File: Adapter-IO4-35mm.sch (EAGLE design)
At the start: 3 parts

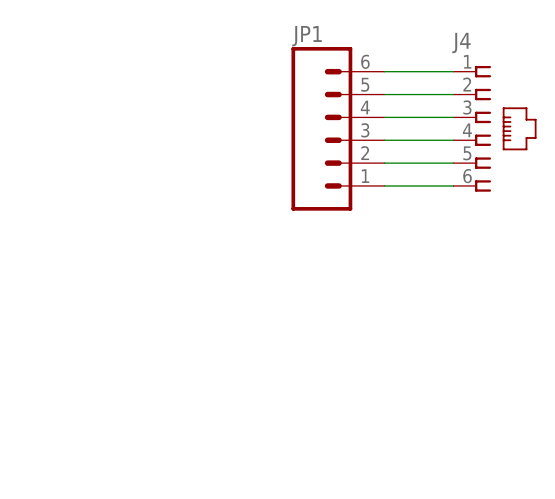
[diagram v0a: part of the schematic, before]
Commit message: added values for connectors
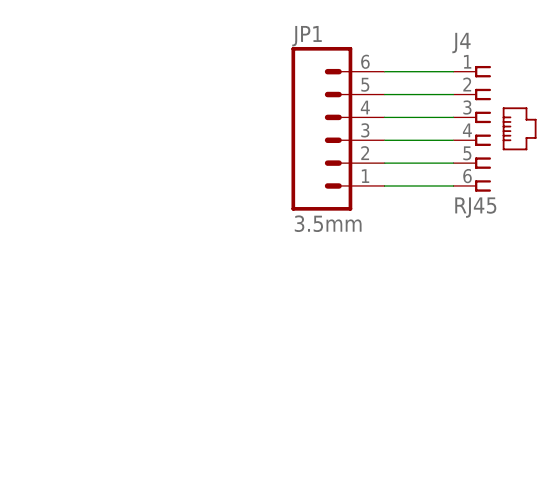
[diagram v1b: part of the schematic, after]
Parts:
- J4: value (none) -> RJ45
- JP1: value (none) -> 3.5mm
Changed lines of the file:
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@@
 <grid distance="100" unitdist="mil" unit="mil" style="dots" multiple="1" display="yes" altdistance="50" altunitdist="mil" altunit="mil"/>
 <layers>
-<layer number="1" name="Top" color="4" fill="1" visible="yes" active="no"/>
-<layer number="2" name="Route2" color="1" fill="3" visible="yes" active="no"/>
-<layer number="3" name="Route3" color="4" fill="3" visible="yes" active="no"/>
-<layer number="14" name="Route14" color="1" fill="6" visible="yes" active="no"/>
-<layer number="15" name="Route15" color="4" fill="6" visible="yes" active="no"/>
-<layer number="16" name="Bottom" color="1" fill="1" visible="yes" active="no"/>
-<layer number="17" name="Pads" color="2" fill="1" visible="yes" active="no"/>
-<layer number="18" name="Vias" color="2" fill="1" visible="yes" active="no"/>
-<layer number="19" name="Unrouted" color="6" fill="1" visible="yes" active="no"/>
-<layer number="20" name="Dimension" color="15" fill="1" visible="yes" active="no"/>
-<layer number="21" name="tPlace" color="7" fill="1" visible="yes" active="no"/>
-<layer number="22" name="bPlace" color="7" fill="1" visible="yes" active="no"/>
-<layer number="23" name="tOrigins" color="15" fill="1" visible="yes" active="no"/>
-<layer number="24" name="bOrigins" color="15" fill="1" visible="yes" active="no"/>
-<layer number="25" name="tNames" color="7" fill="1" visible="yes" active="no"/>
-<layer number="26" name="bNames" color="7" fill="1" visible="yes" active="no"/>
-<layer number="27" name="tValues" color="7" fill="1" visible="yes" active="no"/>
-<layer number="28" name="bValues" color="7" fill="1" visible="yes" active="no"/>
+<layer number="1" name="Top" color="4" fill="1" visible="no" active="no"/>
+<layer number="2" name="Route2" color="1" fill="3" visible="no" active="no"/>
+<layer number="3" name="Route3" color="4" fill="3" visible="no" active="no"/>
+<layer number="14" name="Route14" color="1" fill="6" visible="no" active="no"/>
+<layer number="15" name="Route15" color="4" fill="6" visible="no" active="no"/>
+<layer number="16" name="Bottom" color="1" fill="1" visible="no" active="no"/>
+<layer number="17" name="Pads" color="2" fill="1" visible="no" active="no"/>
+<layer number="18" name="Vias" color="2" fill="1" visible="no" active="no"/>
+<layer number="19" name="Unrouted" color="6" fill="1" visible="no" active="no"/>
+<layer number="20" name="Dimension" color="15" fill="1" visible="no" active="no"/>
+<layer number="21" name="tPlace" color="7" fill="1" visible="no" active="no"/>
+<layer number="22" name="bPlace" color="7" fill="1" visible="no" active="no"/>
+<layer number="23" name="tOrigins" color="15" fill="1" visible="no" active="no"/>
+<layer number="24" name="bOrigins" color="15" fill="1" visible="no" active="no"/>
+<layer number="25" name="tNames" color="7" fill="1" visible="no" active="no"/>
+<layer number="26" name="bNames" color="7" fill="1" visible="no" active="no"/>
+<layer number="27" name="tValues" color="7" fill="1" visible="no" active="no"/>
+<layer number="28" name="bValues" color="7" fill="1" visible="no" active="no"/>
 <layer number="29" name="tStop" color="7" fill="3" visible="no" active="no"/>
 <layer number="30" name="bStop" color="7" fill="6" visible="no" active="no"/>
@@
 <layer number="35" name="tGlue" color="7" fill="4" visible="no" active="no"/>
 <layer number="36" name="bGlue" color="7" fill="5" visible="no" active="no"/>
-<layer number="37" name="tTest" color="7" fill="1" visible="yes" active="no"/>
-<layer number="38" name="bTest" color="7" fill="1" visible="yes" active="no"/>
+<layer number="37" name="tTest" color="7" fill="1" visible="no" active="no"/>
+<layer number="38" name="bTest" color="7" fill="1" visible="no" active="no"/>
 <layer number="39" name="tKeepout" color="4" fill="11" visible="no" active="no"/>
 <layer number="40" name="bKeepout" color="1" fill="11" visible="no" active="no"/>
@@
 <layer number="44" name="Drills" color="7" fill="1" visible="no" active="no"/>
 <layer number="45" name="Holes" color="7" fill="1" visible="no" active="no"/>
-<layer number="46" name="Milling" color="3" fill="1" visible="yes" active="no"/>
-<layer number="47" name="Measures" color="7" fill="1" visible="yes" active="no"/>
-<layer number="48" name="Document" color="7" fill="1" visible="yes" active="no"/>
-<layer number="49" name="Reference" color="7" fill="1" visible="yes" active="no"/>
-<layer number="50" name="dxf" color="7" fill="1" visible="yes" active="no"/>
-<layer number="51" name="tDocu" color="7" fill="1" visible="yes" active="no"/>
-<layer number="52" name="bDocu" color="7" fill="1" visible="yes" active="no"/>
-<layer number="53" name="tGND_GNDA" color="7" fill="9" visible="yes" active="no"/>
-<layer number="54" name="bGND_GNDA" color="1" fill="9" visible="yes" active="no"/>
-<layer number="56" name="wert" color="7" fill="1" visible="yes" active="no"/>
-<layer number="57" name="tCAD" color="7" fill="1" visible="yes" active="no"/>
-<layer number="59" name="tCarbon" color="7" fill="1" visible="yes" active="no"/>
-<layer number="60" name="bCarbon" color="7" fill="1" visible="yes" active="no"/>
+<layer number="46" name="Milling" color="3" fill="1" visible="no" active="no"/>
+<layer number="47" name="Measures" color="7" fill="1" visible="no" active="no"/>
+<layer number="48" name="Document" color="7" fill="1" visible="no" active="no"/>
+<layer number="49" name="Reference" color="7" fill="1" visible="no" active="no"/>
+<layer number="50" name="dxf" color="7" fill="1" visible="no" active="no"/>
+<layer number="51" name="tDocu" color="7" fill="1" visible="no" active="no"/>
+<layer number="52" name="bDocu" color="7" fill="1" visible="no" active="no"/>
+<layer number="53" name="tGND_GNDA" color="7" fill="9" visible="no" active="no"/>
+<layer number="54" name="bGND_GNDA" color="1" fill="9" visible="no" active="no"/>
+<layer number="56" name="wert" color="7" fill="1" visible="no" active="no"/>
+<layer number="57" name="tCAD" color="7" fill="1" visible="no" active="no"/>
+<layer number="59" name="tCarbon" color="7" fill="1" visible="no" active="no"/>
+<layer number="60" name="bCarbon" color="7" fill="1" visible="no" active="no"/>
 <layer number="90" name="Modules" color="5" fill="1" visible="yes" active="yes"/>
 <layer number="91" name="Nets" color="2" fill="1" visible="yes" active="yes"/>
@@
 <part name="FRAME1" library="SparkFun" deviceset="FRAME-LETTER" device=""/>
 <part name="U$1" library="SPCoast" deviceset="DOC-OSHW-LOGO-" device="M" value="DOC-OSHW-LOGO-M"/>
-<part name="JP1" library="SPCoast" deviceset="CONNECTOR-M06" device="3.5MM-6"/>
-<part name="J4" library="SPCoast" deviceset="CONNECTOR-RJ25" device="-6P6C"/>
+<part name="JP1" library="SPCoast" deviceset="CONNECTOR-M06" device="3.5MM-6" value="3.5mm"/>
+<part name="J4" library="SPCoast" deviceset="CONNECTOR-RJ25" device="-6P6C" value="RJ45"/>
 </parts>
 <sheets>

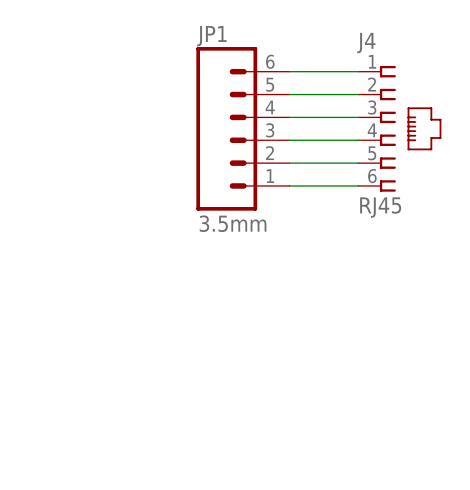
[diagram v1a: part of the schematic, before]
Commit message: normalized values
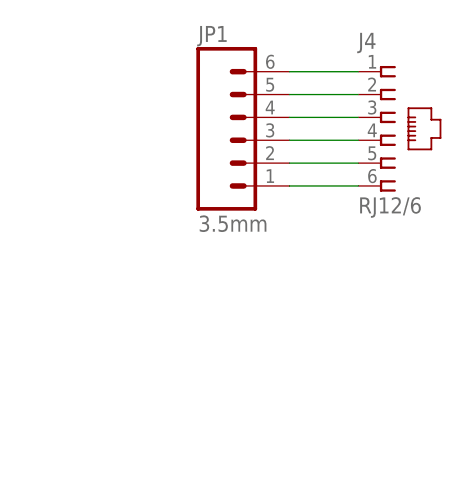
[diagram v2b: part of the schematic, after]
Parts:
- J4: value RJ45 -> RJ12/6
- U$1: value DOC-OSHW-LOGO-M -> OSHW
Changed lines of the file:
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@@
 <parts>
 <part name="FRAME1" library="SparkFun" deviceset="FRAME-LETTER" device=""/>
-<part name="U$1" library="SPCoast" deviceset="DOC-OSHW-LOGO-" device="M" value="DOC-OSHW-LOGO-M"/>
+<part name="U$1" library="SPCoast" deviceset="DOC-OSHW-LOGO-" device="M" value="OSHW"/>
 <part name="JP1" library="SPCoast" deviceset="CONNECTOR-M06" device="3.5MM-6" value="3.5mm"/>
-<part name="J4" library="SPCoast" deviceset="CONNECTOR-RJ25" device="-6P6C" value="RJ45"/>
+<part name="J4" library="SPCoast" deviceset="CONNECTOR-RJ25" device="-6P6C" value="RJ12/6"/>
 </parts>
 <sheets>
